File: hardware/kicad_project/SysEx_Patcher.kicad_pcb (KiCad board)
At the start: 4 copper layers, 172 x 228 mm, 86 parts, among them J1 MIDI_IN, J10 JACK6.35, J2 MIDI_OUT, J3 DC_5V, J4 BAT_PWR, J5 OLED, SW1 prog/MIDI, SW2 SW, SW3 SW, SW4 SW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

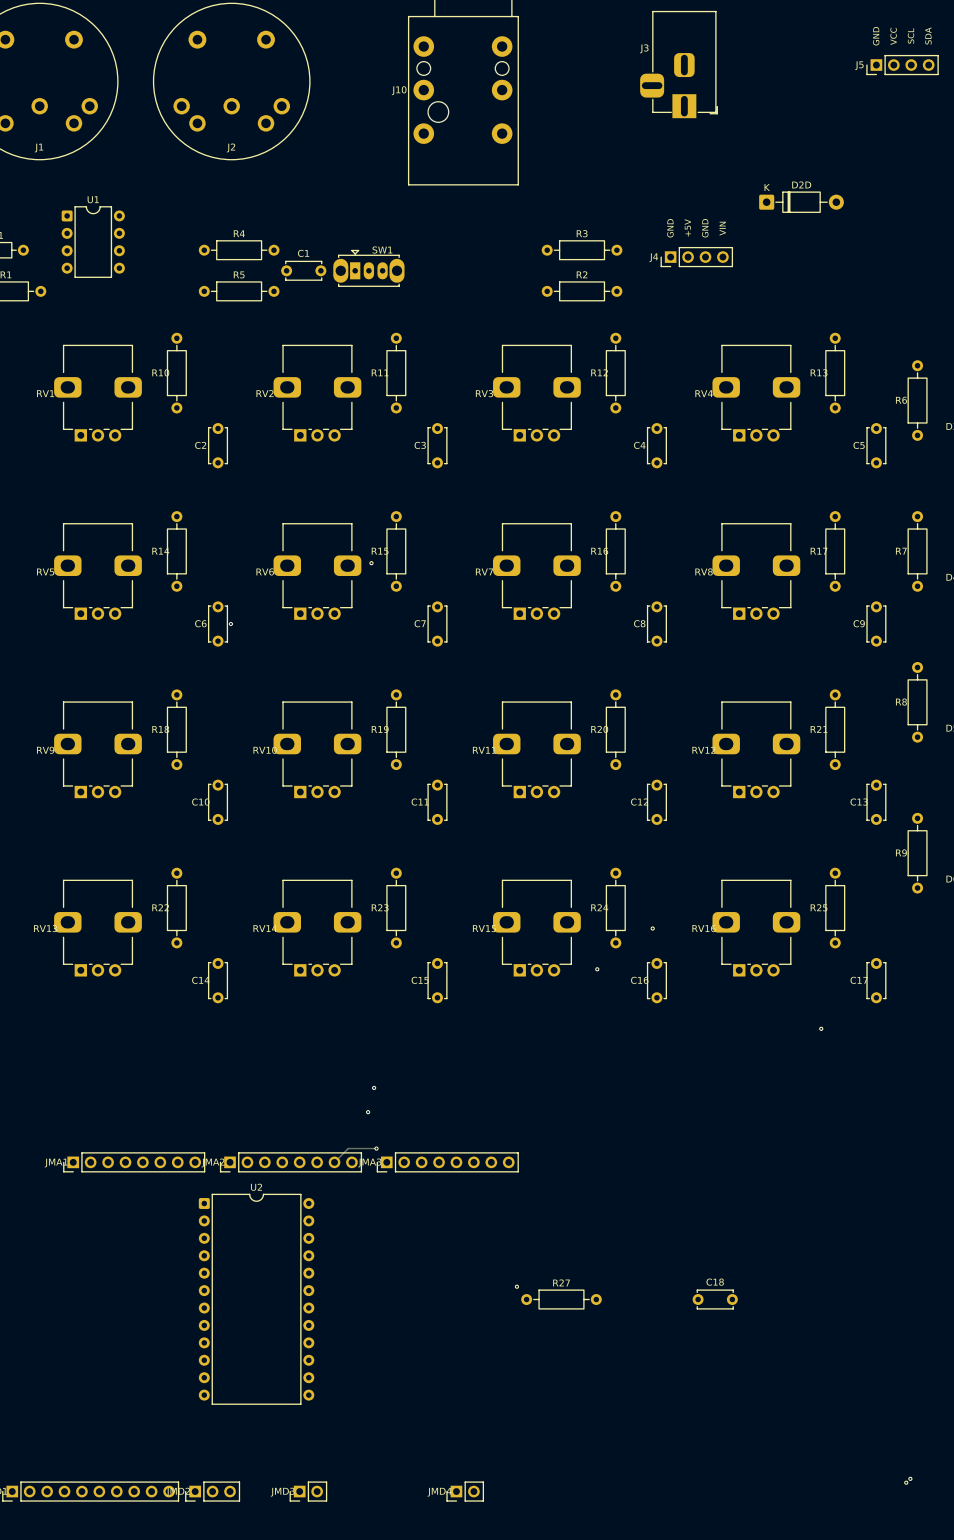
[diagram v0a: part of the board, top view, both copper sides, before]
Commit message: hardware: add polarised 100uF electrolytic (C19) on the +5V rail
- C19 = CP_Radial D6.3mm electrolytic across +5V/GND (pad1 + -> +5V, pad2 - -> GND)
  with silkscreen polarity '+' marker and 100uF value label
- schematic: C19 uses Device:C_Polarized symbol
- reroute 0 unconnected, DRC clean, ERC clean (only the 14 intentional spare
  mux-channel warnings); fab Gerbers, schematic PDF, previews + BOM updated
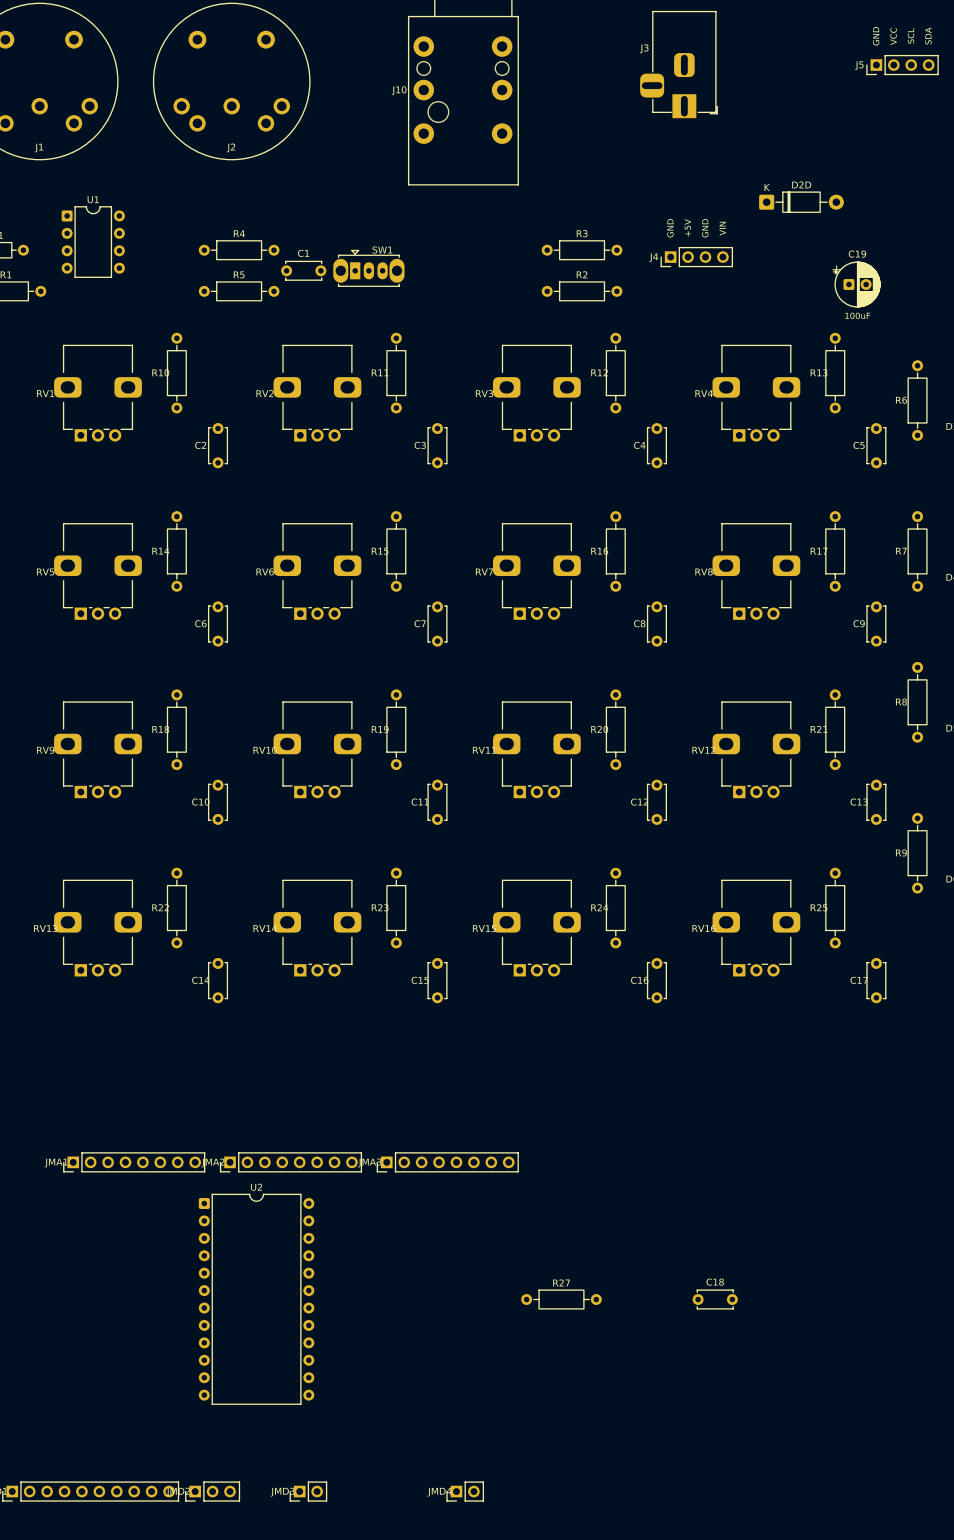
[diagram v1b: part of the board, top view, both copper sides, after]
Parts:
- added C19: 100uF, Capacitor_THT:CP_Radial_D6.3mm_P2.50mm, F.Cu at (142.0, 44.0)
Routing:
- net +5V: track 656.0 -> 0.00 mm
- net D12: track 252.5 -> 0.00 mm, vias 1 -> 0
- net D20_SDA: track 241.4 -> 0.00 mm
- net D11: track 237.2 -> 0.00 mm, vias 1 -> 0
- net D21_SCL: track 234.4 -> 0.00 mm
- net VIN_RAW: track 227.2 -> 0.00 mm, vias 1 -> 0
- net D10: track 216.7 -> 0.00 mm, vias 1 -> 0
- net D1_TX: track 203.8 -> 0.00 mm
- net D0_RX: track 181.1 -> 0.00 mm
- net JACK_W: track 176.2 -> 0.00 mm, vias 1 -> 0
- net A12: track 169.6 -> 0.00 mm, vias 1 -> 0
- net D7: track 169.3 -> 0.00 mm
- net D9: track 162.9 -> 0.00 mm
- net A8: track 157.5 -> 0.00 mm, vias 1 -> 0
- net D8: track 151.8 -> 0.00 mm
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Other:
- board text added: "+"
- board text added: "100uF"

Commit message: hardware: move 4067 mux (U2) beside the Mega + align board within sheet frame
- U2 (and R27/C18) relocated to the free area to the RIGHT of the Arduino Mega
  instead of sitting in the gap between the header rows (i.e. under the Mega)
- shift all board geometry by (20,20) so the PCB sits inside the KiCad drawing
  sheet frame instead of hanging off the page corner
- reroute: 0 unconnected, DRC clean; fab Gerbers + previews regenerated
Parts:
- moved U2 91.8 mm to (138.0, 196.0)
- moved R27 73.7 mm to (168.0, 202.0)
- moved C18 53.7 mm to (168.0, 216.0)
- moved JMA1 28.3 mm to (48.9, 192.0)
- moved JMA2 28.3 mm to (71.8, 192.0)
- moved JMA3 28.3 mm to (94.6, 192.0)
- moved JMD2 28.3 mm to (66.7, 240.0)
- moved C1 28.3 mm to (80.0, 62.0)
- moved C10 28.3 mm to (70.0, 142.0)
- moved C11 28.3 mm to (102.0, 142.0)
- moved C12 28.3 mm to (134.0, 142.0)
- moved C13 28.3 mm to (166.0, 142.0)
- moved C14 28.3 mm to (70.0, 168.0)
- moved C15 28.3 mm to (102.0, 168.0)
- moved C16 28.3 mm to (134.0, 168.0)
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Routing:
- net +5V: track 0.00 -> 682.9 mm, vias 0 -> 1
- net D20_SDA: track 0.00 -> 243.9 mm
- net D21_SCL: track 0.00 -> 234.4 mm
- net D12: track 0.00 -> 229.8 mm, vias 0 -> 1
- net VIN_RAW: track 0.00 -> 221.2 mm, vias 0 -> 1
- net JACK_W: track 0.00 -> 216.1 mm, vias 0 -> 1
- net D11: track 0.00 -> 212.4 mm, vias 0 -> 1
- net D1_TX: track 0.00 -> 200.2 mm
- net D10: track 0.00 -> 196.6 mm, vias 0 -> 1
- net D0_RX: track 0.00 -> 187.9 mm
- net D7: track 0.00 -> 175.8 mm
- net A12: track 0.00 -> 163.0 mm, vias 0 -> 1
- net D9: track 0.00 -> 152.6 mm
- net D8: track 0.00 -> 148.4 mm
- net A8: track 0.00 -> 139.2 mm
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
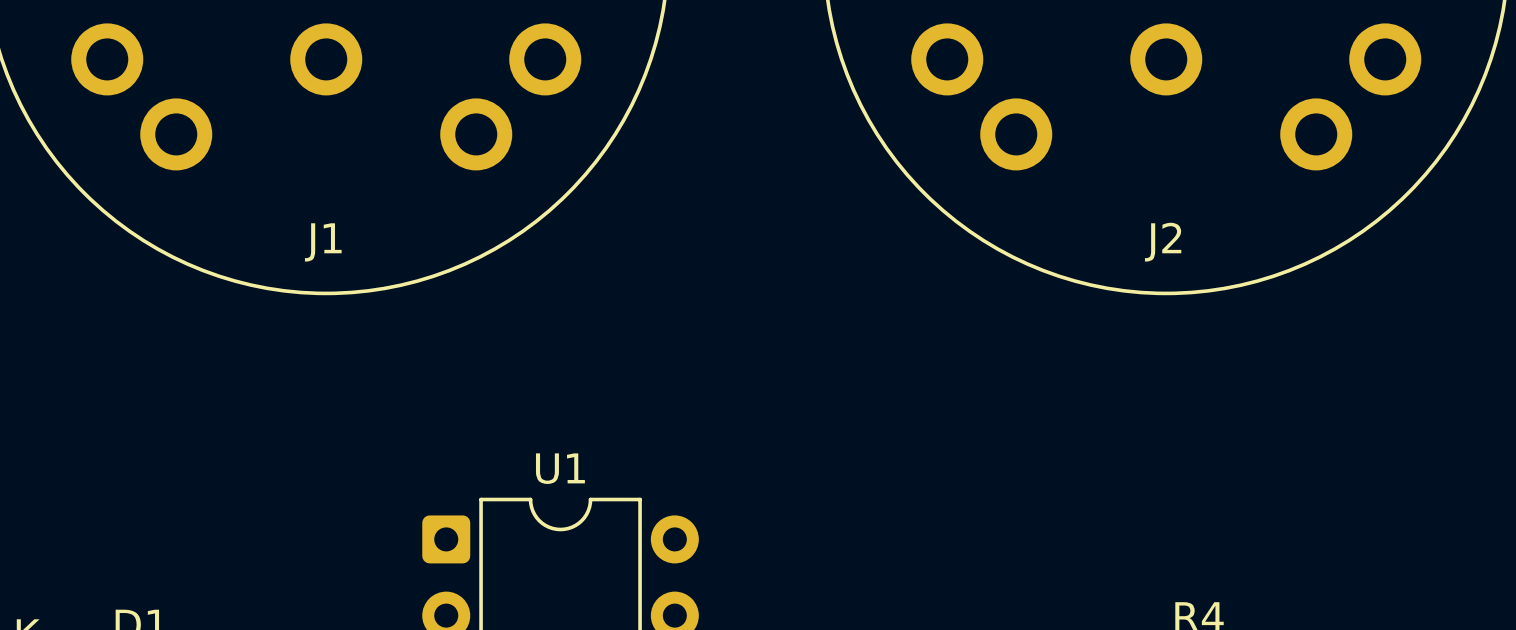
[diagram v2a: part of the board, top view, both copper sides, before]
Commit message: hardware: add "MIDI IN"/"MIDI OUT" silkscreen labels on J1/J2
Reroute 0 unconnected, DRC clean; fab Gerbers + previews regenerated.
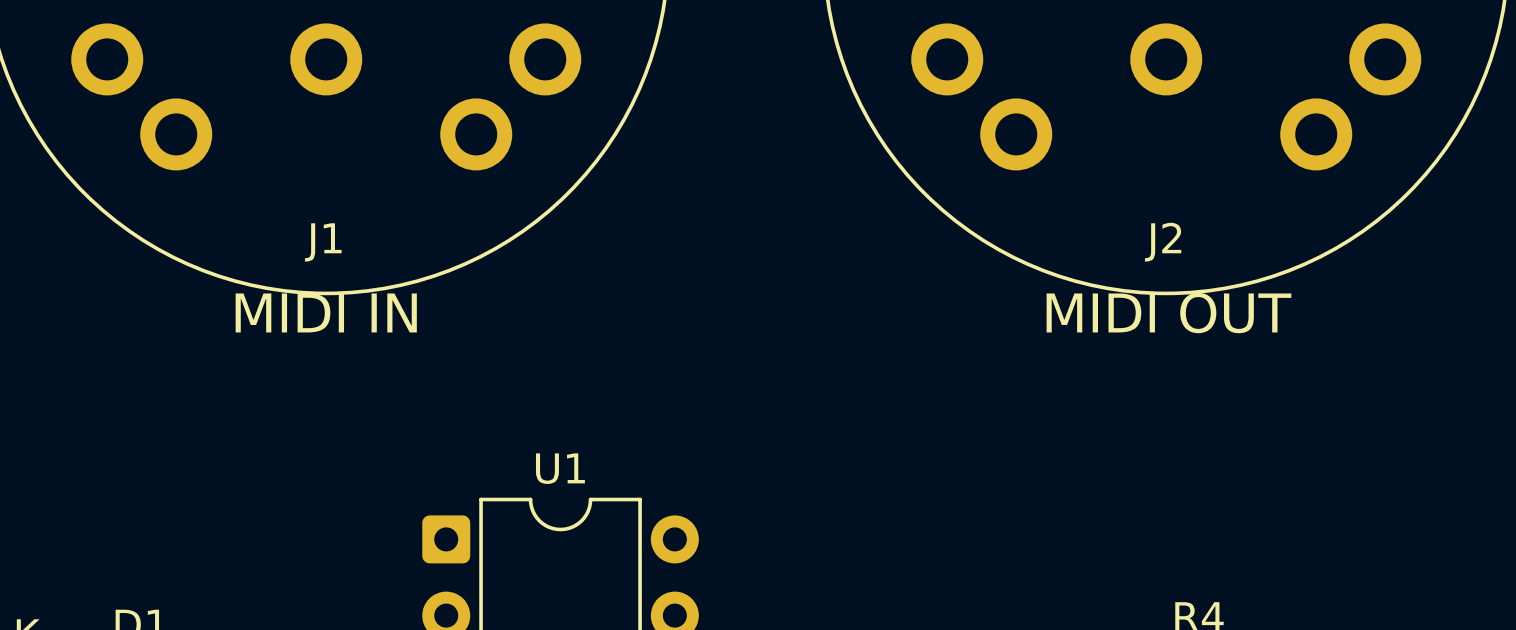
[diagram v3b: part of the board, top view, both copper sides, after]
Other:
- board text added: "MIDI IN"
- board text added: "MIDI OUT"

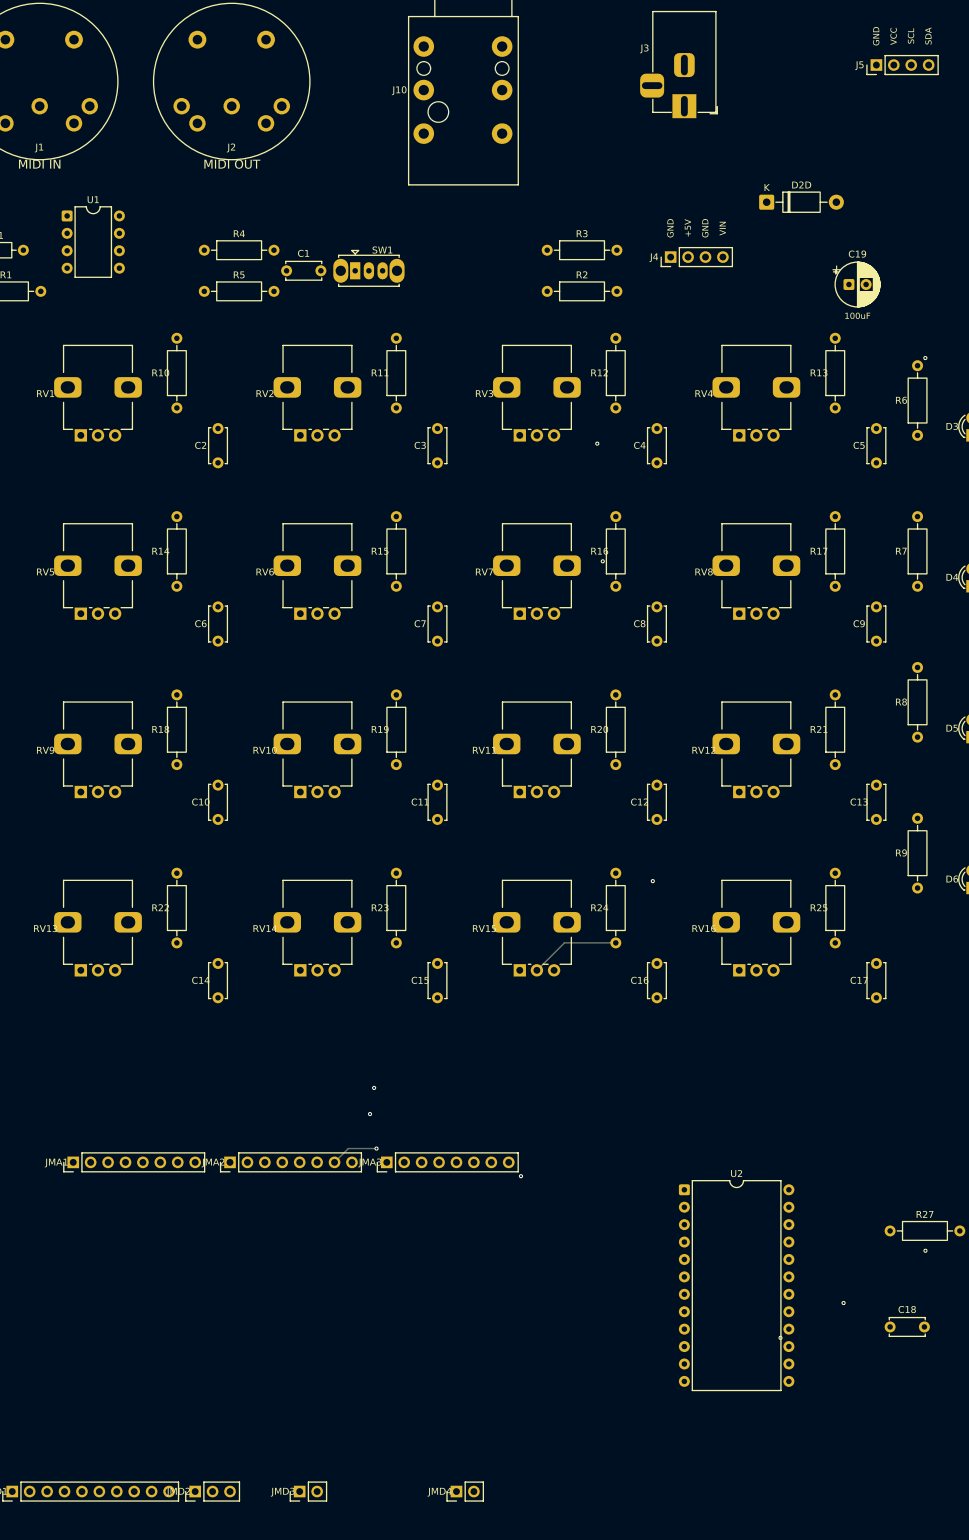
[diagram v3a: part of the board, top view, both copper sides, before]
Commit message: hardware: clean, fully-wired schematic (organized by functional block)
Replace the flat label-on-pin schematic with a readable single-sheet design:
- components grouped into titled blocks (power, MIDI IN/OUT, jack, buttons,
  LEDs, OLED, mux, Mega headers, 16 pot RC filters)
- power symbols (+5V/GND) and net labels on wired stubs
- each of the 16 pots drawn as a wired RC filter cell (pot -> 1k series ->
  100nF to GND, wiper + ADC node labelled)
- ERC clean except the 14 intentional spare 4067 mux-channel labels
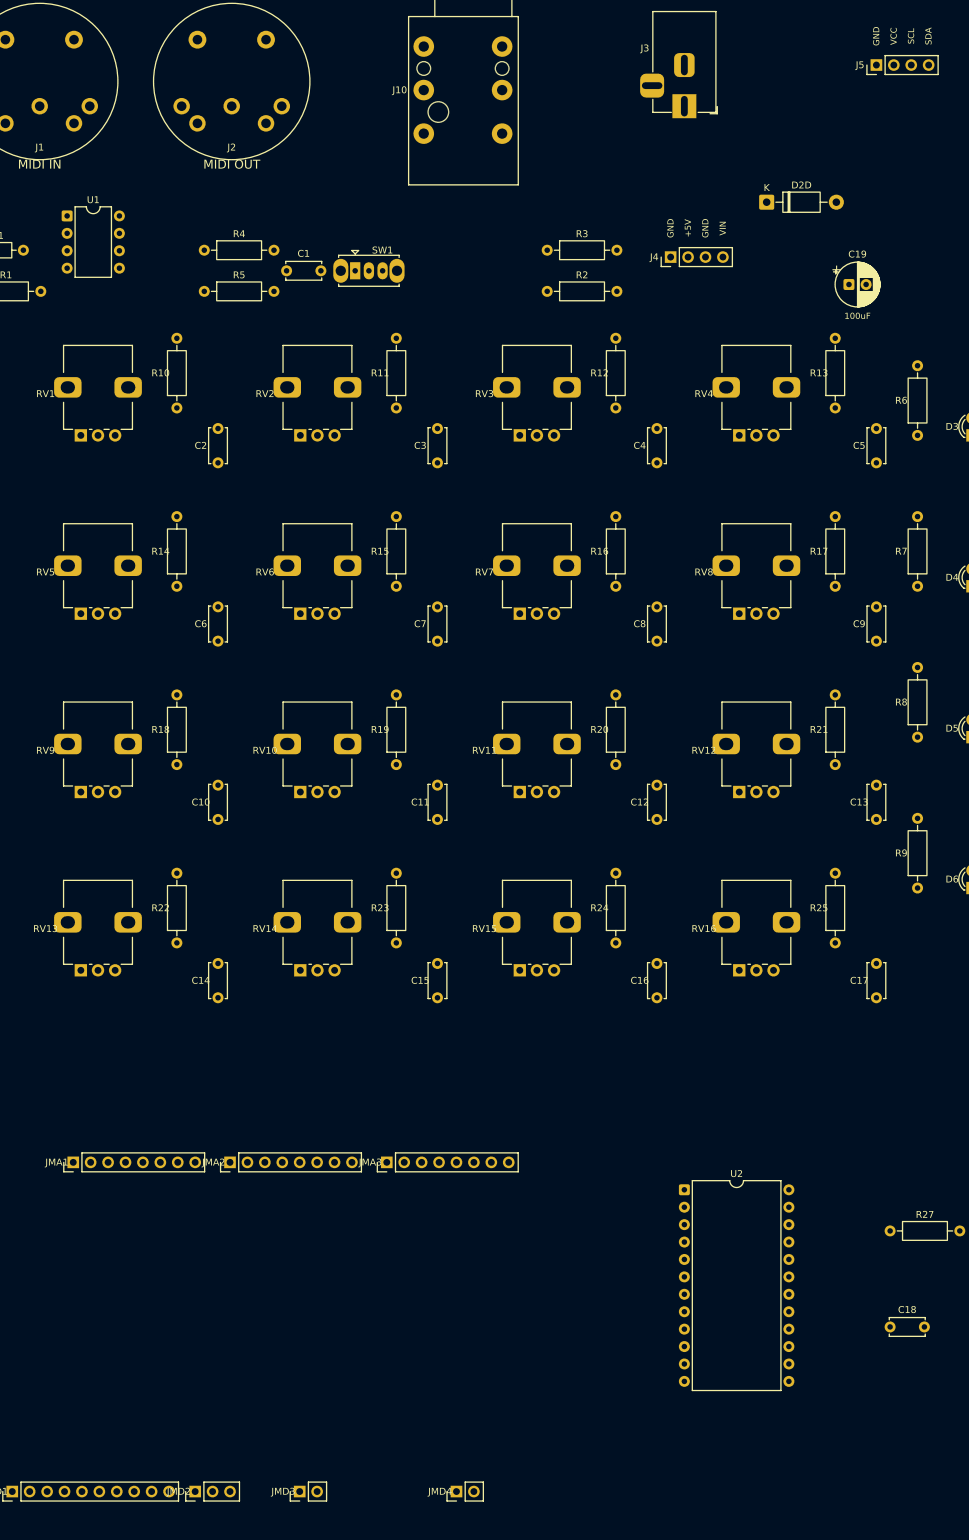
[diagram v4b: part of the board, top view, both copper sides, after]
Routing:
- net +5V: track 682.9 -> 0.00 mm, vias 1 -> 0
- net D20_SDA: track 243.9 -> 0.00 mm
- net D21_SCL: track 234.4 -> 0.00 mm
- net D12: track 229.8 -> 0.00 mm, vias 1 -> 0
- net VIN_RAW: track 221.2 -> 0.00 mm, vias 1 -> 0
- net JACK_W: track 216.1 -> 0.00 mm, vias 1 -> 0
- net D11: track 212.4 -> 0.00 mm, vias 1 -> 0
- net D1_TX: track 200.2 -> 0.00 mm
- net D10: track 196.6 -> 0.00 mm, vias 1 -> 0
- net D0_RX: track 187.9 -> 0.00 mm
- net D7: track 175.8 -> 0.00 mm
- net A12: track 163.0 -> 0.00 mm, vias 1 -> 0
- net D9: track 152.6 -> 0.00 mm
- net D8: track 148.4 -> 0.00 mm
- net A8: track 139.2 -> 0.00 mm
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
